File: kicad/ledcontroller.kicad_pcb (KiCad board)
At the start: 2 copper layers, 90.5 x 56 mm, 51 parts, among them J1 USB_A, J2 HLJ-6115ANL, J3 STELVIO-2P-508, J4 STELVIO-2P-508, J5 STELVIO-2P-508, J6 STELVIO-3P-508, J7 STELVIO-3P-508, P1 FDI_Cable, P2 CONN_02X02, Q1 IRLU2905PBF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

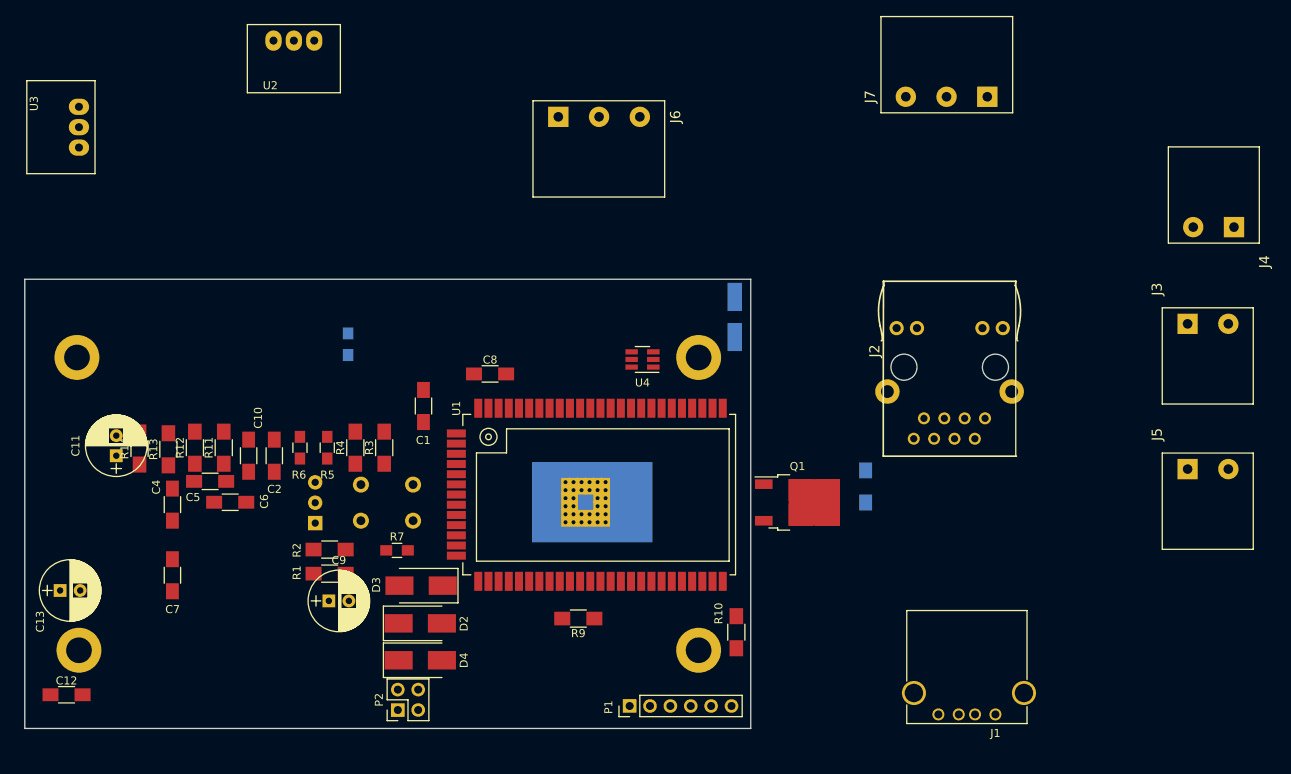
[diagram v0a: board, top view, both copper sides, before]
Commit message: PCB: Basic placement and initial routing ok
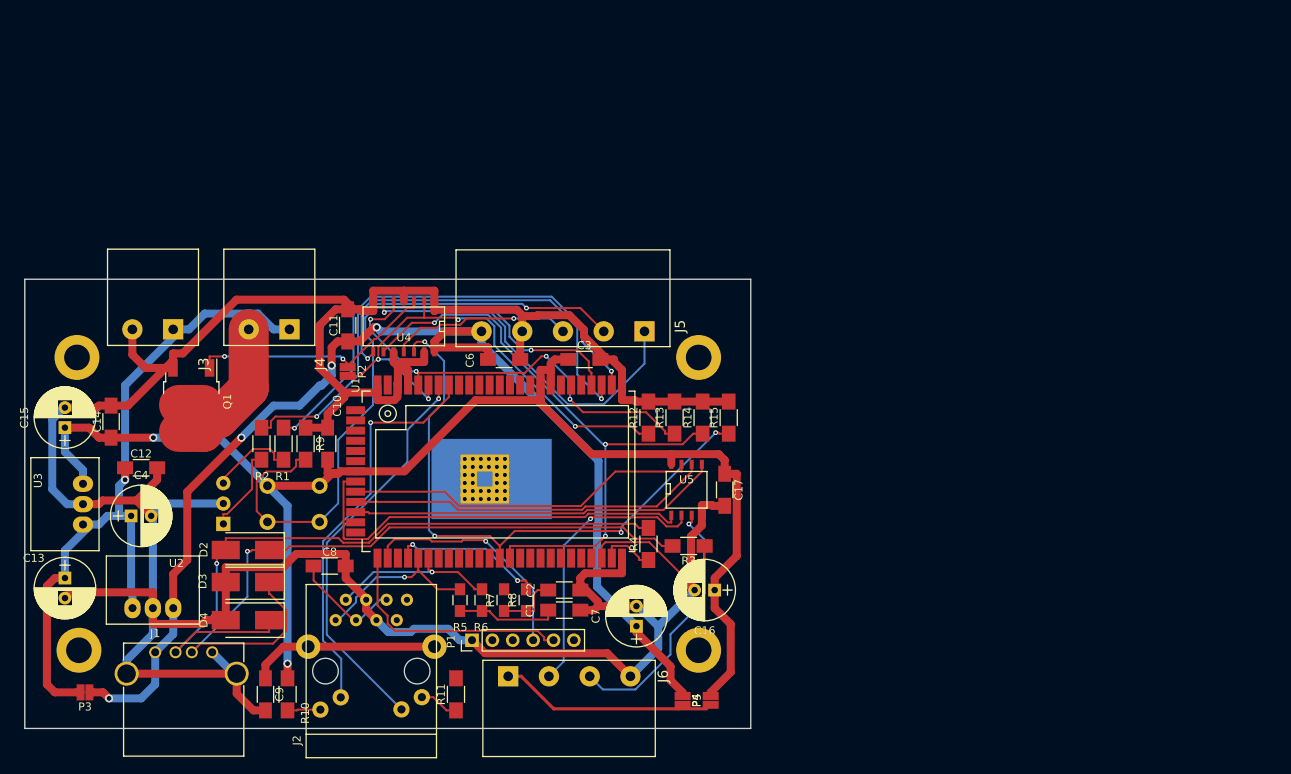
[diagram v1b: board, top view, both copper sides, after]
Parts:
- removed C5: 1uF, Capacitors_SMD:C_1206_HandSoldering
- removed D5: STPS1L30A, Diodes_SMD:D_SMA_Handsoldering
- removed J7: STELVIO-3P-508, plan44:STELVIO-3P-508
- added C14: 100nF, Capacitors_SMD:C_1206_HandSoldering, F.Cu at (82.8, 81.8)
- added C15: 22uF 25V, Capacitors_ThroughHole:CP_Radial_D7.5mm_P2.50mm, F.Cu at (77.0, 82.5)
- added C16: 10uF, Capacitors_ThroughHole:CP_Radial_D7.5mm_P2.50mm, F.Cu at (158.0, 102.8)
- added C17: 100nF, Capacitors_SMD:C_1206_HandSoldering, F.Cu at (159.2, 90.2)
- added P3: CONN_01X02, plan44:CONFIG-PAD-2P, F.Cu at (79.5, 115.5)
- added P4: CONN_01X02, plan44:CONFIG-PAD-2P, F.Cu at (157.5, 116.5)
- added P5: CONN_01X02, plan44:CONFIG-PAD-2P, F.Cu at (154.0, 116.5)
- added R15: 100k, Resistors_SMD:R_1206_HandSoldering, F.Cu at (159.8, 81.2)
- added U5: MCP3002, SMD_Packages:SOIC-8-N, F.Cu at (154.5, 90.2)
- C11: value 10uF 50VDC -> 100nF; footprint Capacitors_ThroughHole:CP_Radial_D7.5mm_P2.50mm -> Capacitors_SMD:C_1206_HandSoldering
- C13: value 22uF 25V -> 10uF 50VDC
- C3, R8: moved to F.Cu
- C4: value 100nF -> 10uF 50VDC; footprint Capacitors_SMD:C_1206_HandSoldering -> Capacitors_ThroughHole:CP_Radial_D7.5mm_P2.50mm
- C7: value 100nF -> 22uF 25V; footprint Capacitors_SMD:C_1206_HandSoldering -> Capacitors_ThroughHole:CP_Radial_D7.5mm_P2.50mm
- C8: value 100nF -> 1uF
- C9: value 10uF -> 1nF/2kV; footprint Capacitors_ThroughHole:CP_Radial_D7.5mm_P2.50mm -> Capacitors_SMD:C_1206_HandSoldering
- J2: value HLJ-6115ANL -> Pulse-J0026D21B; footprint plan44:HLJ-6115ANL -> plan44:PULSE-J0026D21B
- J5: value STELVIO-2P-508 -> STELVIO-5P-508; footprint plan44:STELVIO-2P-508 -> plan44:STELVIO-5P-508
- J6: value STELVIO-3P-508 -> STELVIO-4P-508; footprint plan44:STELVIO-3P-508 -> plan44:STELVIO-4P-508
- P2: value CONN_02X02 -> CONN_01X02; footprint Pin_Headers:Pin_Header_Straight_2x02_Pitch2.54mm -> plan44:CONFIG-PAD-2P
- R13, R14: value 10k -> 100k
- U2: value Recom_R78Cxx -> Recom_R785.0-0.5
- U3: value 74AHCT1G125 -> Recom_R783.3-0.5
- U4: value MCP3421A0T-E/CH -> 74AHCT125; footprint TO_SOT_Packages_SMD:SOT-23-6_Handsoldering -> SMD_Packages:SOIC-14_N
- moved J3 157.0 mm to (75.2, 70.2), turned to 0 degrees
- moved J4 118.4 mm to (89.8, 70.2)
- moved J1 105.0 mm to (88.2, 110.5), turned to 0 degrees
- moved J5 84.7 mm to (149.2, 70.5), turned to 0 degrees
- moved J2 83.8 mm to (110.8, 106.5), turned to 180 degrees
- moved Q1 76.6 mm to (92.8, 79.2), turned to 270 degrees
- moved U2 71.8 mm to (90.5, 105.0), turned to 180 degrees
- moved R14 70.3 mm to (156.5, 81.2)
- moved J6 70.0 mm to (147.5, 113.5)
- moved R13 63.2 mm to (153.0, 81.2)
- moved C7 58.2 mm to (148.2, 107.2)
- moved R12 56.7 mm to (149.8, 81.2)
- moved R10 56.5 mm to (104.8, 115.8), turned to 90 degrees
- moved U3 47.0 mm to (79.2, 89.5)
- moved P2 42.7 mm to (112.2, 75.5)
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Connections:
- net Net-(J4-Pad2) renamed /FET_PWR
- C10 pad 1: +24V -> +3V3
- C11 pad 1: +24V -> +5V
- C12 pad 1: +3V3 -> +24V
- C13 pad 1: +3V3 -> +24V
- C4 pad 1: +3V3 -> +24V
- C6 pad 1: +3V3 -> +5V
- C8 pad 1: +3V3 -> Net-(C8-Pad1)
- C9 pad 1: +3V3 -> /CHS_GND
- J2 pad 11: Net-(J2-Pad11) -> /WLAN_LED
- J2 pad 12: /WLAN_LED -> Net-(J2-Pad12)
- J2 pad 3: /ETH0_RX+ -> Net-(C8-Pad1)
- J2 pad 4: Net-(C5-Pad1) -> GND
- J2 pad 5: Net-(C5-Pad1) -> GND
- J2 pad 6: /ETH0_RX- -> Net-(C8-Pad1)
- J2 pad 7: /ETH_PWR+ -> /ETH0_RX+
- J2 pad 8: /ETH_PWR- -> /ETH0_RX-
- J2 pad S1: GND -> /CHS_GND
- J2 pad S2: GND -> /CHS_GND
- J5 pad 1: +5V -> /LED_DATA1
- J5 pad 2: GND -> /LED_DATA2
- J6 pad 1: +5V -> /SENS_PWR
- J6 pad 2: (no net) -> Net-(J6-Pad2)
- J6 pad 3: GND -> Net-(J6-Pad3)
- P2 pad 1: /PPoE+ -> /LED_FET_3V
- P2 pad 2: /ETH_PWR+ -> /LED_FET_5V
- Q1 pad 1: /LEDPWR1 -> /LED_FET_5V
- R11 pad 1: Net-(J2-Pad11) -> Net-(J2-Pad12)
- R12 pad 1: /LEDPWR1 -> /LED_FET_3V
- R13 pad 1: /I2C_SDA -> /LED_DATA1_3V
- R13 pad 2: +3V3 -> GND
- R14 pad 1: +3V3 -> /LED_DATA2_3V
- R14 pad 2: /I2C_SCL -> GND
- U1 pad A10: (no net) -> /SPI_MISO
- U1 pad A11: (no net) -> /SPI_MOSI
- U1 pad A5: /I2C_SCL -> (no net)
- U1 pad A6: /I2C_SDA -> (no net)
- U1 pad A8: (no net) -> /SPI_CS1
- U1 pad A9: (no net) -> /SPI_CLK
- U1 pad B13: (no net) -> /LED_DATA3_3V
- U1 pad B14: (no net) -> /LED_DATA2_3V
- U1 pad C5: /LEDS1_DATA_3V -> /LED_DATA1_3V
- U1 pad C6: /LEDPWR1 -> /LED_FET_3V
- U2 pad 3: +3V3 -> +5V
- U3 pad 1: GND -> +24V
- U3 pad 2: /LEDS1_DATA_3V -> GND
- U3 pad 3: GND -> +3V3
- U4 pad 1: Net-(J7-Pad2) -> GND
- U4 pad 2: GND -> /LED_FET_3V
- U4 pad 3: /I2C_SCL -> /LED_FET_5V
- U4 pad 4: /I2C_SDA -> GND
- U4 pad 5: +3V3 -> /LED_DATA1_3V
- U4 pad 6: GND -> /LED_DATA1
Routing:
- net GND: track 0.00 -> 394.1 mm
- net +3V3: track 0.00 -> 174.3 mm, vias 0 -> 2
- net +5V: track 0.00 -> 154.2 mm, vias 0 -> 4
- net Net-(D2-Pad1): track 0.00 -> 90.5 mm, vias 0 -> 1
- net +24V: track 0.00 -> 89.6 mm, vias 0 -> 1
- net Net-(D2-Pad2): track 0.00 -> 85.1 mm, vias 0 -> 1
- net Net-(R9-Pad2): track 0.00 -> 83.5 mm, vias 0 -> 1
- net /LED_DATA2_3V: track 0.00 -> 75.4 mm, vias 0 -> 3
- net /LED_DATA3_3V: track 0.00 -> 73.8 mm, vias 0 -> 4
- net Net-(R2-Pad1): track 0.00 -> 64.1 mm, vias 0 -> 2
- net /LED_FET_3V: track 0.00 -> 61.1 mm, vias 0 -> 4
- net Net-(R1-Pad1): track 0.00 -> 58.4 mm, vias 0 -> 2
- net /LED_DATA1_3V: track 0.00 -> 54.0 mm, vias 0 -> 4
- net /SPI_CS1: track 0.00 -> 52.1 mm
- net /ETH0_LED: track 0.00 -> 50.3 mm, vias 0 -> 1
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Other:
- net class PowerFET added: clearance 0.2, trace_width 5, via_dia 1, via_drill 0.6

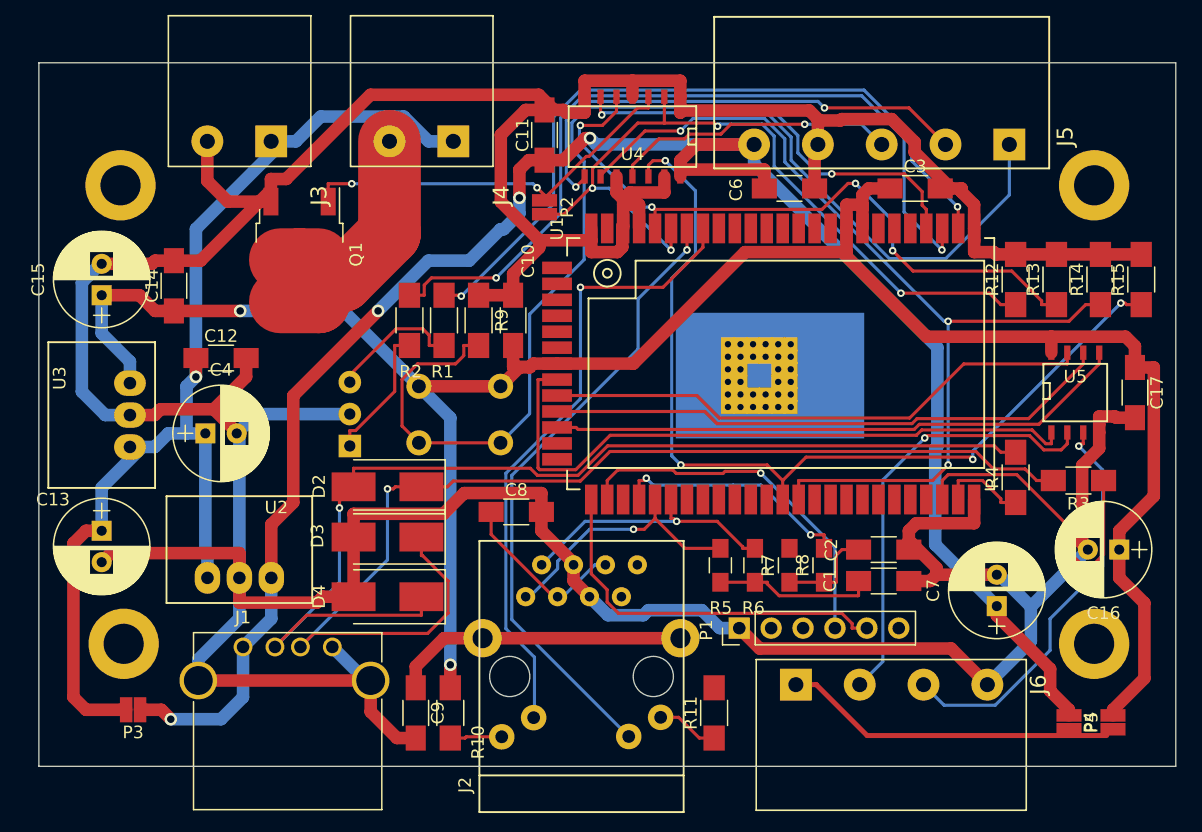
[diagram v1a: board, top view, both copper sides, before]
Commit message: First completely routed version including zones for Power FET
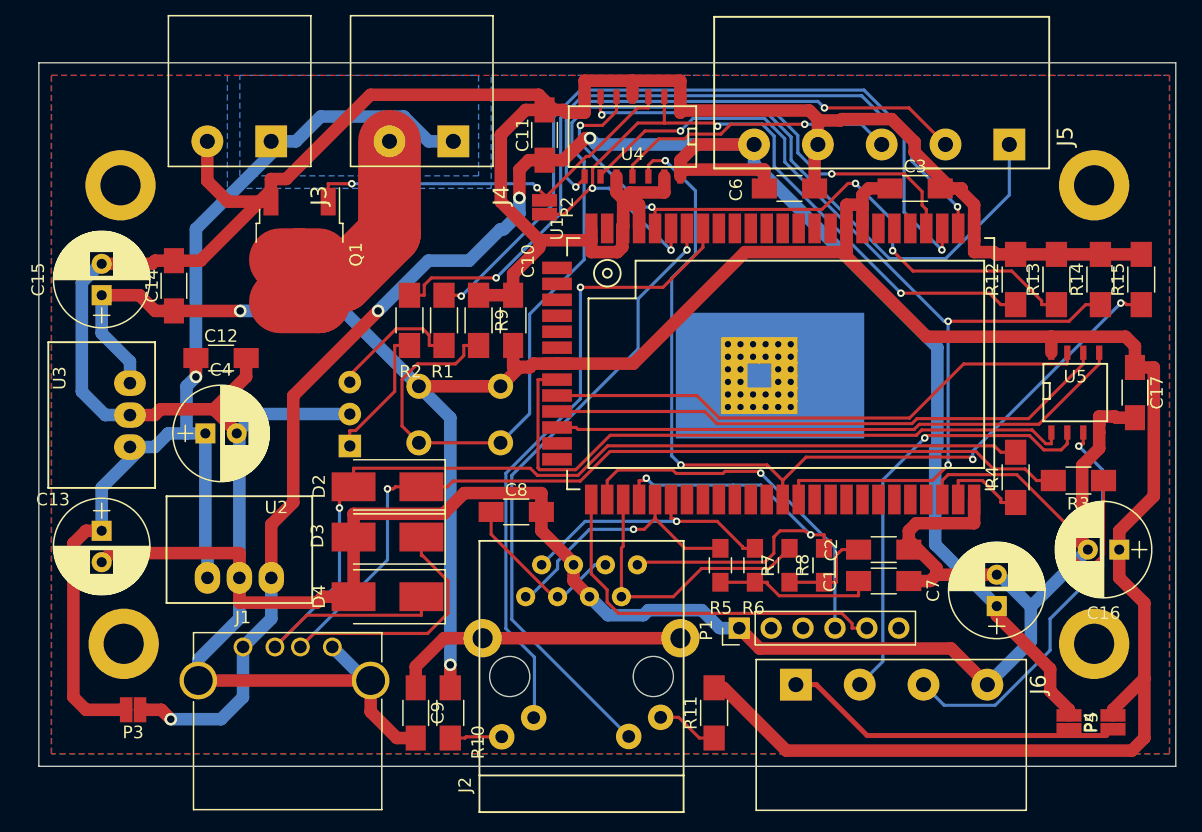
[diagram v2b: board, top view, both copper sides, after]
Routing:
- net +3V3: track 174.3 -> 215.8 mm
- net /ETH0_RX+: track 0.47 -> 23.2 mm
- net /ETH0_RX-: track 19.3 -> 35.1 mm
- added copper zone on B.Cu, net +24V
- added copper zone on B.Cu, net GND
- added copper zone on F.Cu, net GND
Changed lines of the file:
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@@
   (general
     (links 140)
-    (no_connects 4)
-    (area 71.949999 63.949999 162.550001 120.050001)
+    (no_connects 0)
+    (area 29.114287 35.4 171.600001 131.650001)
     (thickness 1.6)
-    (drawings 19)
-    (tracks 707)
+    (drawings 20)
+    (tracks 727)
     (zones 0)
     (modules 57)
@@
     )
   )
+  (dimension 6 (width 0.3) (layer Dwgs.User)
+    (gr_text "0.2362 in" (at 93 55.65) (layer Dwgs.User)
+      (effects (font (size 1.5 1.5) (thickness 0.3)))
+    )
+    (feature1 (pts (xy 96 79) (xy 96 54.3)))
+    (feature2 (pts (xy 90 79) (xy 90 54.3)))
+    (crossbar (pts (xy 90 57) (xy 96 57)))
+    (arrow1a (pts (xy 96 57) (xy 94.873496 57.586421)))
+    (arrow1b (pts (xy 96 57) (xy 94.873496 56.413579)))
+    (arrow2a (pts (xy 90 57) (xy 91.126504 57.586421)))
+    (arrow2b (pts (xy 90 57) (xy 91.126504 56.413579)))
+  )
   (gr_line (start 67.8 123.7) (end 171.5 123.7) (angle 90) (layer Dwgs.User) (width 0.2))
   (gr_line (start 165.7 60.3) (end 165.6 60.4) (angle 90) (layer Dwgs.User) (width 0.2))
@@
   (segment (start 135.4753 105.35) (end 135.4753 103.1994) (width 0.25) (layer F.Cu) (net 3))
   (segment (start 134.5 105.35) (end 135.4753 105.35) (width 0.25) (layer F.Cu) (net 3))
+  (segment (start 125.75 113.75) (end 126.5 113.75) (width 1) (layer F.Cu) (net 4))
+  (segment (start 126.5 113.75) (end 131.5 118.75) (width 1) (layer F.Cu) (net 4))
+  (segment (start 131.5 118.75) (end 159 118.75) (width 1) (layer F.Cu) (net 4))
+  (segment (start 159 118.75) (end 160 117.75) (width 1) (layer F.Cu) (net 4))
+  (segment (start 160 117.75) (end 160 113) (width 1) (layer F.Cu) (net 4))
   (segment (start 158 102.75) (end 158 105) (width 1) (layer F.Cu) (net 4))
   (segment (start 160 113) (end 157.5 115.5) (width 1) (layer F.Cu) (net 4))
@@
   (segment (start 115.4801 100.4999) (end 122.7646 100.4999) (width 0.25) (layer B.Cu) (net 12))
   (segment (start 112.02 103.96) (end 115.4801 100.4999) (width 0.25) (layer B.Cu) (net 12))
+  (segment (start 118.37 106.5) (end 122.5 106.5) (width 0.25) (layer F.Cu) (net 13))
+  (segment (start 130.15 104.25) (end 131.75 102.65) (width 0.25) (layer F.Cu) (net 13))
+  (segment (start 124.75 104.25) (end 130.15 104.25) (width 0.25) (layer F.Cu) (net 13))
+  (segment (start 122.5 106.5) (end 124.75 104.25) (width 0.25) (layer F.Cu) (net 13))
+  (segment (start 118.51 98.7625) (end 118.51 102.49) (width 0.25) (layer F.Cu) (net 13))
+  (segment (start 118.37 102.63) (end 118.37 106.5) (width 0.25) (layer F.Cu) (net 13))
+  (segment (start 118.51 102.49) (end 118.37 102.63) (width 0.25) (layer F.Cu) (net 13))
   (segment (start 118.7056 106.1644) (end 118.37 106.5) (width 0.25) (layer F.Cu) (net 13))
+  (segment (start 133.4341 101.5747) (end 133.3247 101.5747) (width 0.25) (layer F.Cu) (net 14))
+  (segment (start 129.799998 103.75) (end 119.85 103.75) (width 0.25) (layer F.Cu) (net 14))
+  (segment (start 130.506801 103.043197) (end 129.799998 103.75) (width 0.25) (layer F.Cu) (net 14))
+  (segment (start 130.506801 101.743199) (end 130.506801 103.043197) (width 0.25) (layer F.Cu) (net 14))
+  (segment (start 131 101.25) (end 130.506801 101.743199) (width 0.25) (layer F.Cu) (net 14))
+  (segment (start 133 101.25) (end 131 101.25) (width 0.25) (layer F.Cu) (net 14))
+  (segment (start 133.3247 101.5747) (end 133 101.25) (width 0.25) (layer F.Cu) (net 14))
+  (segment (start 119.85 103.75) (end 119.64 103.96) (width 0.25) (layer F.Cu) (net 14))
   (via (at 120.3541 97.0668) (size 0.6) (layers F.Cu B.Cu) (net 14))
   (via (at 133.4341 101.5747) (size 0.6) (layers F.Cu B.Cu) (net 14))
@@
   (segment (start 132.26 113.5) (end 133.8803 113.5) (width 0.4) (layer F.Cu) (net 43))
   (segment (start 157 117.55) (end 153.5 117.55) (width 0.4) (layer F.Cu) (net 43))
+  (zone (net 2) (net_name GND) (layer F.Cu) (hatch edge 0.508)
+    (connect_pads (clearance 0.508))
+    (min_thickness 0.254)
+    (fill yes (arc_segments 16) (thermal_gap 0.508) (thermal_bridge_width 0.508))
+    (polygon
+      (pts
+        (xy 162 119) (xy 73 119) (xy 73 65) (xy 162 65)
+      )
+    )
+  )
+  (zone (net 5) (net_name +24V) (layer B.Cu) (hatch edge 0.508)
+    (connect_pads yes (clearance 0.508))
+    (min_thickness 0.254)
+    (fill yes (arc_segments 16) (thermal_gap 0.508) (thermal_bridge_width 0.508))
+    (polygon
+      (pts
+        (xy 107 73) (xy 88 73) (xy 88 65) (xy 107 65)
+      )
+    )
+  )
+  (zone (net 2) (net_name GND) (layer B.Cu) (hatch edge 0.508)
+    (connect_pads (clearance 0.508))
+    (min_thickness 0.254)
+    (fill yes (arc_segments 16) (thermal_gap 0.508) (thermal_bridge_width 0.508))
+    (polygon
+      (pts
+        (xy 87 74) (xy 108 74) (xy 108 65) (xy 162 65) (xy 162 119)
+        (xy 73 119) (xy 73 65) (xy 87 65)
+      )
+    )
+  )
 )
